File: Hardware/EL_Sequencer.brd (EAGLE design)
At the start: 57.1 x 82.5 mm, 109 parts, among them J1 Battery, J2 DC-OUTPUT, J3 AC-INPUT, U1 LM317, U10 Z0103MN, U11 Z0103MN, U12 Z0103MN, U13 MOC3063S, U14 MOC3063S, U15 MOC3063S, U16 MOC3063S, U17 Z0103MN, U18 Z0103MN, U19 Z0103MN, U2 MIC5219-3.3, U20 Z0103MN, U3 ATMEGA328P, U4-DNP XBEE HEADER, U5 MOC3063S, U6 MOC3063S, U7 MOC3063S, U8 MOC3063S, U9 Z0103MN, Y1 8MHz

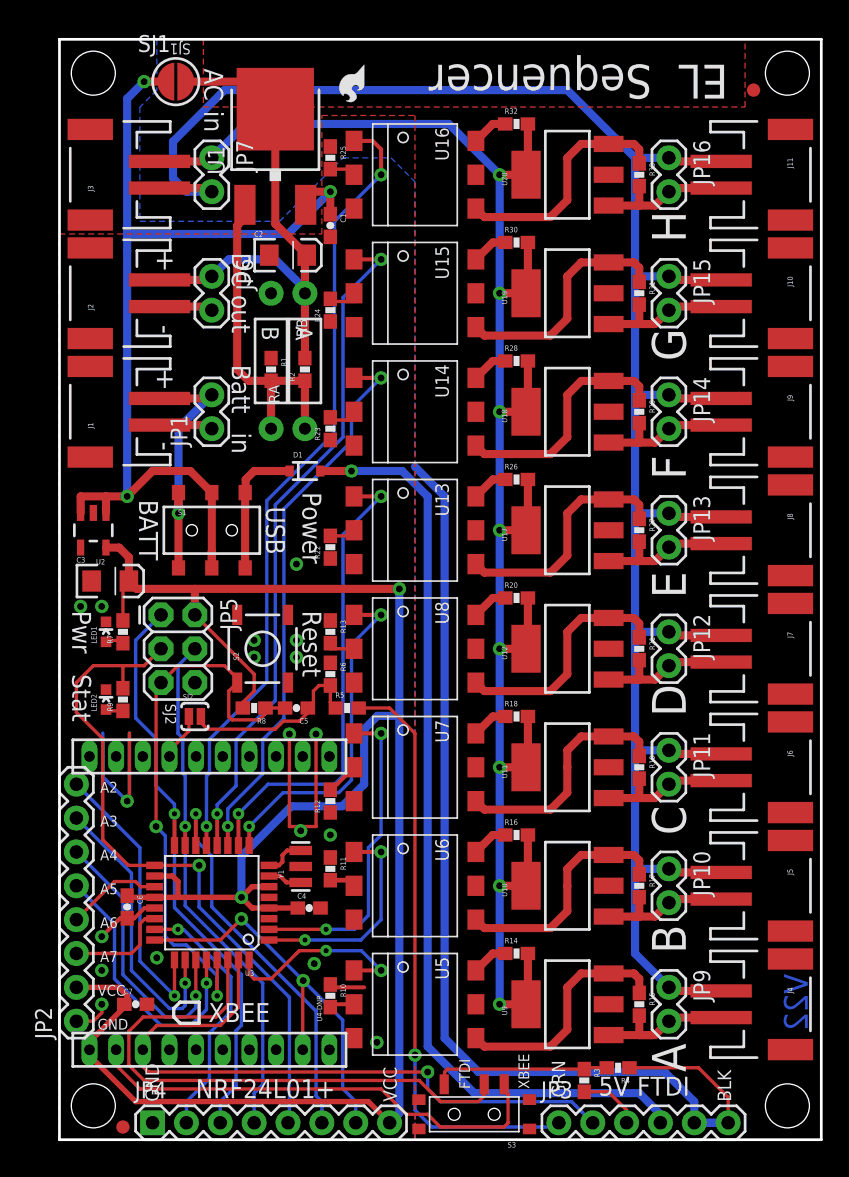
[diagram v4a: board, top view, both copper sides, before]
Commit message: Updates to V2.3
> Swapped LED resistors LED1 (green) now has 470, LED2 (red) now has 1K
> Added heatsink pours for 3.3V reg U2
> Reworked FTDI/XBEE switch, throw is now in direction of respective
connectors, swapped silk, added silk to bottom
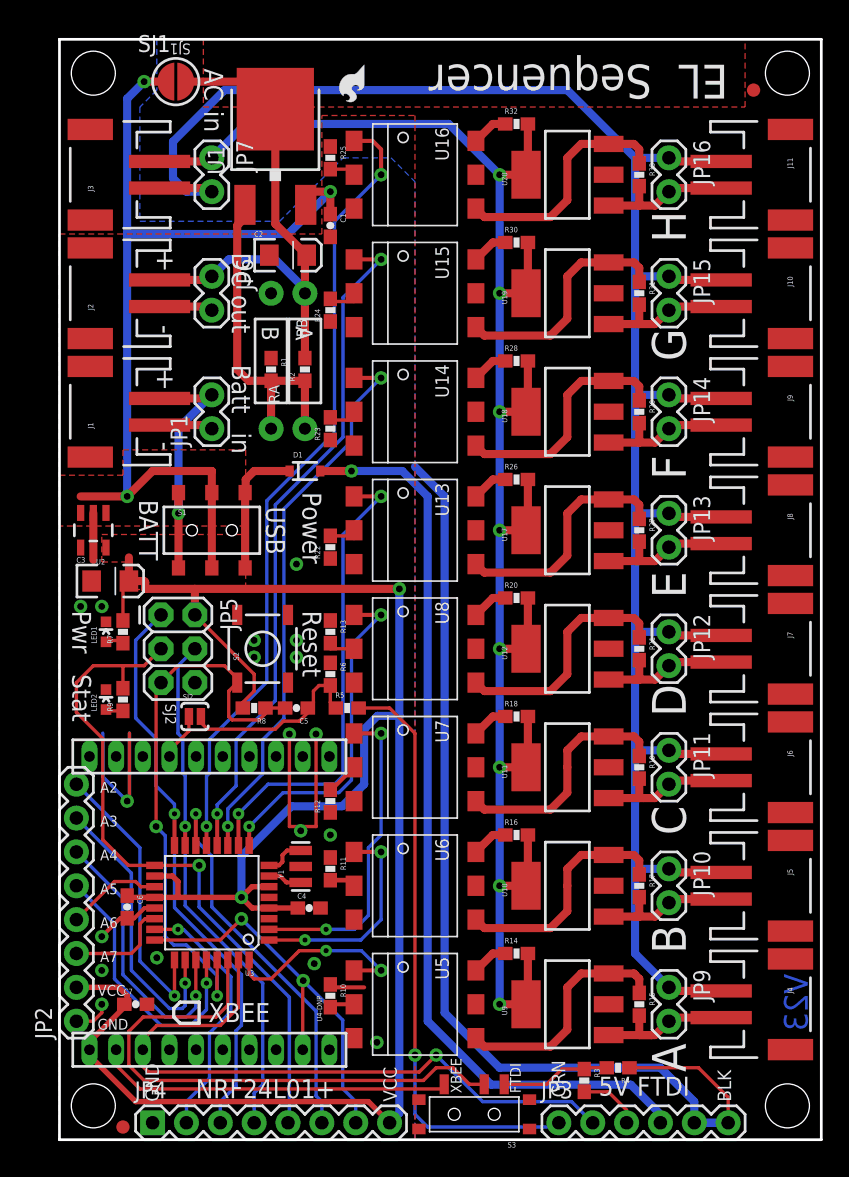
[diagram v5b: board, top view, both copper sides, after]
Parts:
- LED1: value Power -> Power (green)
- LED2: value Status -> STAT(RED)
- R7: value 1K -> 470
- R9: value 470 -> 1K
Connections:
- net RXI_FTDI: now also S3.S; no longer S3.O
- net RXI_XBEE: now also S3.O; no longer S3.S
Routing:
- net RXI_XBEE: track 35.7 -> 26.9 mm
- net RXI_FTDI: track 13.2 -> 8.21 mm
- net RAW: track 74.5 -> 71.7 mm
- net GND: track 129.5 -> 131.9 mm
- net VCC: track 154.2 -> 152.5 mm
- net 5VUSB: track 70.3 -> 69.2 mm
- net RXI: track 43.0 -> 42.2 mm
- added copper zone on layer 1, net RAW
- added copper zone on layer 1, net VCC
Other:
- board text added: "V23"
- board text removed: "V22"

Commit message: Updating parts to proper libraries, swapped stat LED to blue
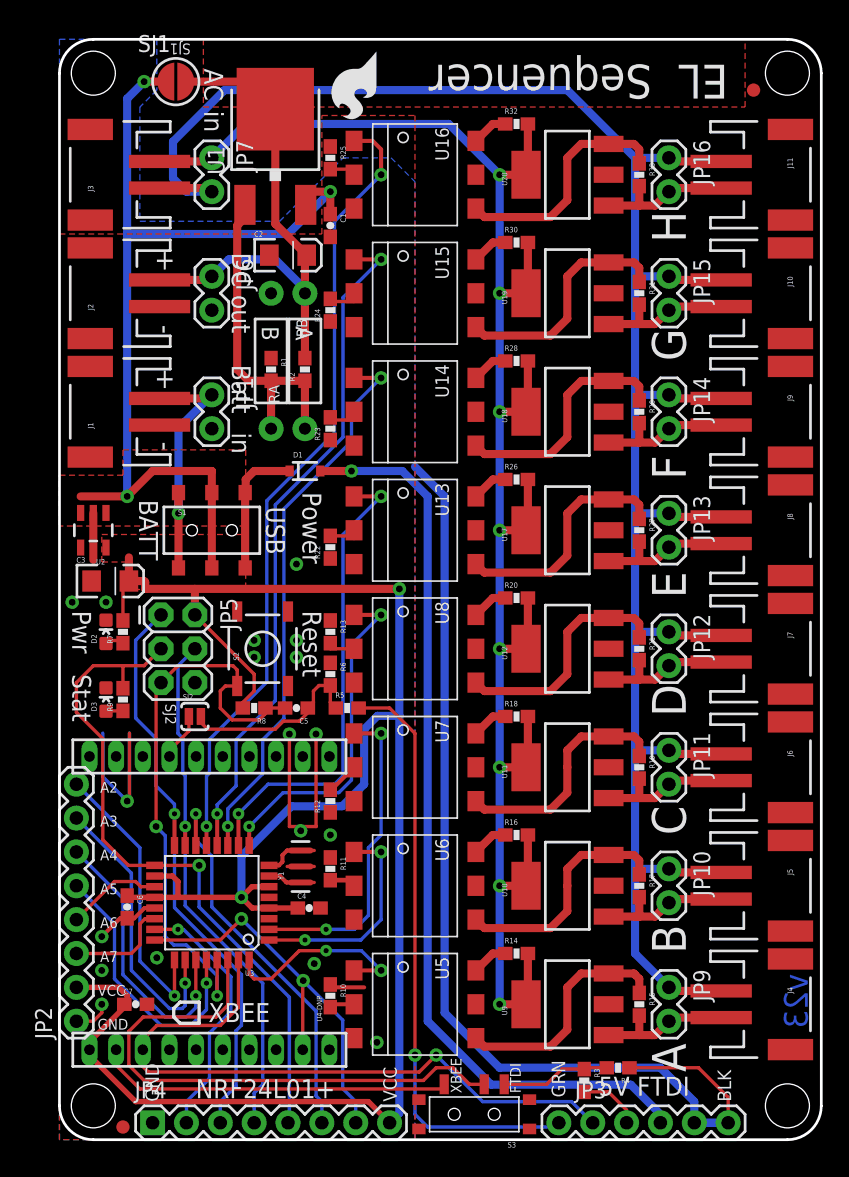
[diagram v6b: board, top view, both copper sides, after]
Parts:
- removed LED1: Power (green), SparkFun:LED-0603
- removed LED2: STAT(RED), SparkFun:LED-0603
- added D2: RED, SparkFun-LED:LED-0603
- added D3: BLUE, SparkFun-LED:LED-0603
- J1, J2, J3: device SparkFun:JST-2-SMD -> SparkFun-Connectors:JST-2-SMD
- J10, J11, J4, J5, J6, J7, J8, J9: value (none) -> M02-JST-2MM-SMT; device SparkFun:JST-2-SMD -> SparkFun-Connectors:JST-2-SMD
- JP1, JP10, JP11, JP12, JP13, JP14, JP15, JP16, JP6, JP7, JP9: value (none) -> M02PTH; device SparkFun:1X02 -> SparkFun-Connectors:1X02
- JP2: device mike-temp:1X08_ROUND -> SparkFun-Connectors:1X08_ROUND
- JP3: device SparkFun:1X06 -> SparkFun-Connectors:FTDI_BASIC
- JP4: device SparkFun:1X08 -> SparkFun-Connectors:1X08
- JP5: device SparkFun:2X3 -> SparkFun-Connectors:2X3
- JP8: value LOGO-SFESK -> SFE_LOGO_FLAME.2_INCH; device SparkFun-Aesthetics:SFE-LOGO-FLAME -> SparkFun-Aesthetics:SFE_LOGO_FLAME_.2
- R7: value 470 -> 1K
- RA, RB: device SparkFun:AXIAL-0.4 -> SparkFun-Resistors:AXIAL-0.4
- S1: value POWER -> DPDT; device SparkFun:AYZ0202 -> SparkFun-Electromechanical:AYZ0202
- S2: device SparkFun:TACTILE_SWITCH_SMD -> SparkFun-Electromechanical:TACTILE-SWITCH-SMD
- SJ1: value (none) -> JUMPER-PAD-2-NOROUND; device mike-temp:SJ_ROUND -> SparkFun-Passives:PAD-JUMPER-2-NO_YES_SILK_ROUND
- SJ2: value (none) -> JUMPER-PAD-2-NOYES_SILK; device SparkFun-Passives:SJ_2S-NO -> SparkFun-Passives:PAD-JUMPER-2-NO_YES_SILK
- U$1: value OSHW-LOGOS -> OSHW-LOGOM; device SparkFun-Aesthetics:OSHW-LOGO-S -> SparkFun-Aesthetics:OSHW-LOGO-M
- U$2: value LOGO-SFENEW -> SFE_LOGO_NAME_FLAME.2_INCH; device SparkFun:SFE-NEW-WEBLOGO -> SparkFun-Aesthetics:SFE_LOGO_NAME_FLAME_.2
- U$5, U$6, U$7, U$8: device SparkFun:STAND-OFF -> SparkFun-Electromechanical:STAND-OFF
- U1: device SparkFun:V-REG_DPACK -> SparkFun-PowerIC:V-REG_DPACK
- U10, U11, U12, U17, U18, U19, U20, U9: device mike-temp:SOT223 -> SparkFun-DiscreteSemi:SOT223
- U13, U14, U15, U16, U5, U6, U7, U8: device mike-temp:DIP8SMD -> SparkFun-DiscreteSemi:DIP8SMD
- U2: value MIC5219-3.3 -> MIC5219 3.3V; device SparkFun:SOT23-5 -> SparkFun-PowerIC:SOT23-5
- U3: device SparkFun:TQFP32-08 -> SparkFun-DigitalIC:TQFP32-08
- U4-DNP: device mike-temp:XBEE-LONGPAD -> SparkFun-RF:XBEE-LONGPAD
- Y1: value 8MHz -> 8MHZ; device SparkFun:RESONATOR-SMD -> SparkFun-FreqCtrl:RESONATOR-SMD
- moved JP1 2.54 mm to (11.4, 55.9), turned to 270 degrees
- moved JP8 1.80 mm to (24.1, 81.9)
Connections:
- net 5VUSB: now also JP3.VCC; no longer JP3.4
- net FTDI_DTR: now also JP3.DTR; no longer JP3.1
- net FTDI_RXI: now also JP3.TXO; no longer JP3.3
- net GND: now also D2.C, D3.C, JP1.2, JP3.CTS, JP3.GND; no longer JP1.1, JP3.5, JP3.6, LED1.C, LED2.C
- net N$14: now also D3.A; no longer LED2.A
- net N$4: now also D2.A; no longer LED1.A
- net TXO: now also JP3.RXI; no longer JP3.2
- net VBATT: now also JP1.1; no longer JP1.2
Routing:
- net GND: track 131.9 -> 124.3 mm
- net RST: track 43.5 -> 44.9 mm
- net N$21: track 11.4 -> 10.4 mm
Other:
- outline, holes or cut-outs redrawn
- board text added: "-M Grusin"
- board text added: "v23"
- board text removed: "M Grusin"
- board text removed: "V23"

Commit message: Fixing issues from QC check
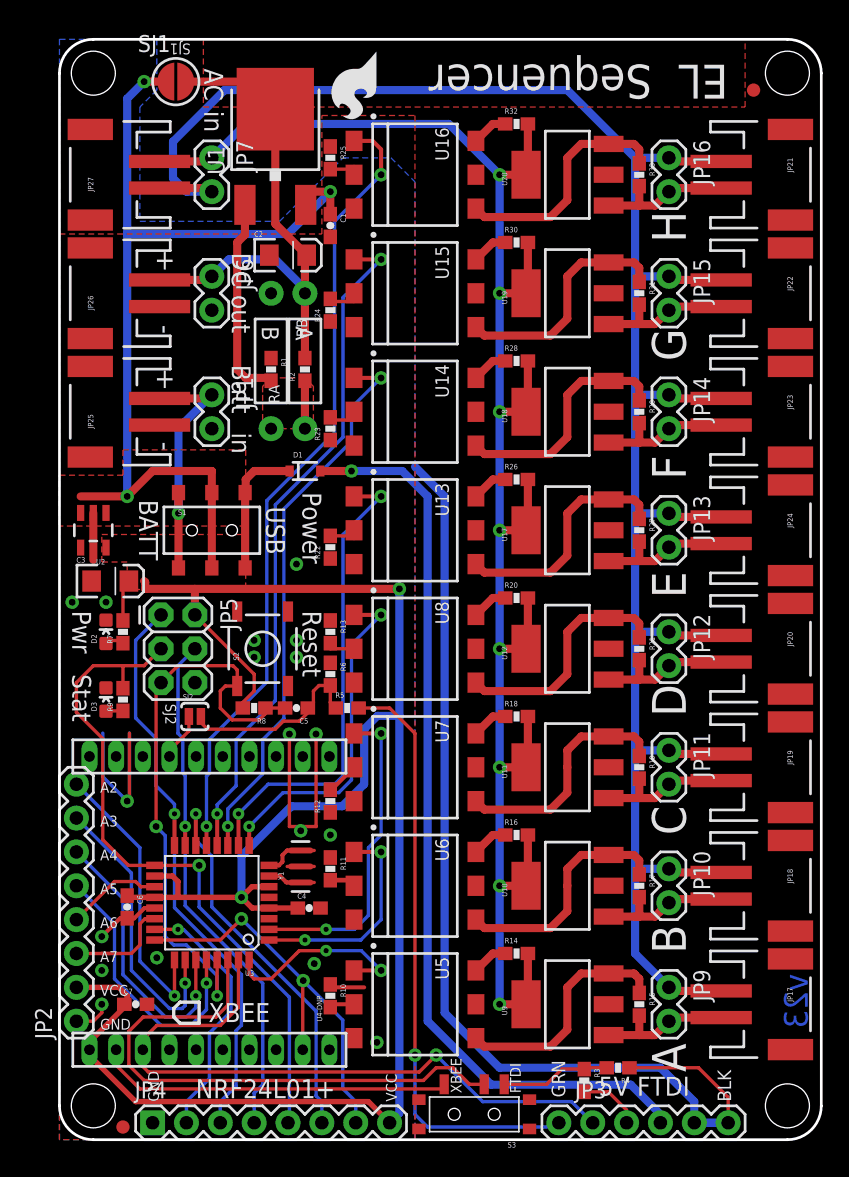
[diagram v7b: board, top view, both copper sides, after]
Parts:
- renumbered J1 to JP25, J10 to JP22, J11 to JP21, J2 to JP26, J3 to JP27, J4 to JP17, J5 to JP18, J6 to JP19, J7 to JP20, J8 to JP24, J9 to JP23
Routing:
- net N$38: track 25.2 -> 19.1 mm
- net VCC: track 152.5 -> 149.6 mm
- added copper zone on layer 1, net N$38
